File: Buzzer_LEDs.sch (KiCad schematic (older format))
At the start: 24 parts, among them Q1 2N7002BK, Q2 BS250P

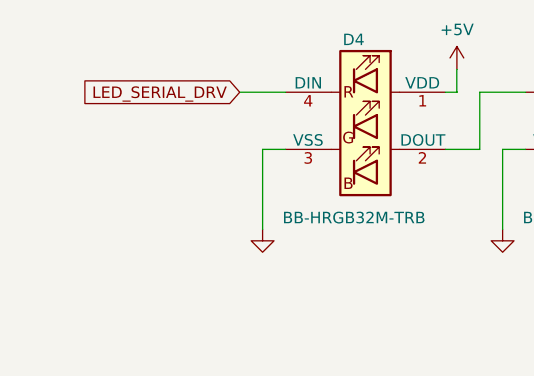
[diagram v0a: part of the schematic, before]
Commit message: changed label on LED Drive for 5V
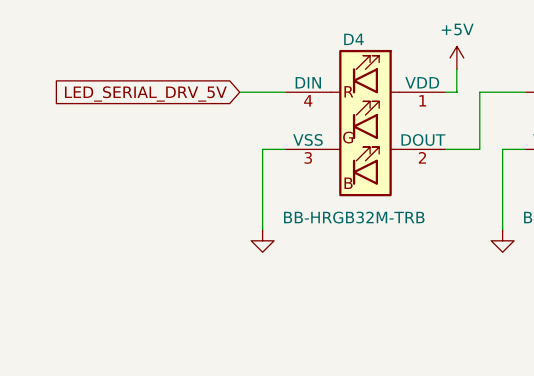
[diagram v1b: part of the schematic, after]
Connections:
- net LED_SERIAL_DRV renamed LED_SERIAL_DRV_5V
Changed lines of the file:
@@
 	2900 1875 2750 1875
 Text GLabel 1850 1625 0    50   Input ~ 0
-LED_SERIAL_DRV
+LED_SERIAL_DRV_5V
 Wire Wire Line
 	2050 1625 1850 1625

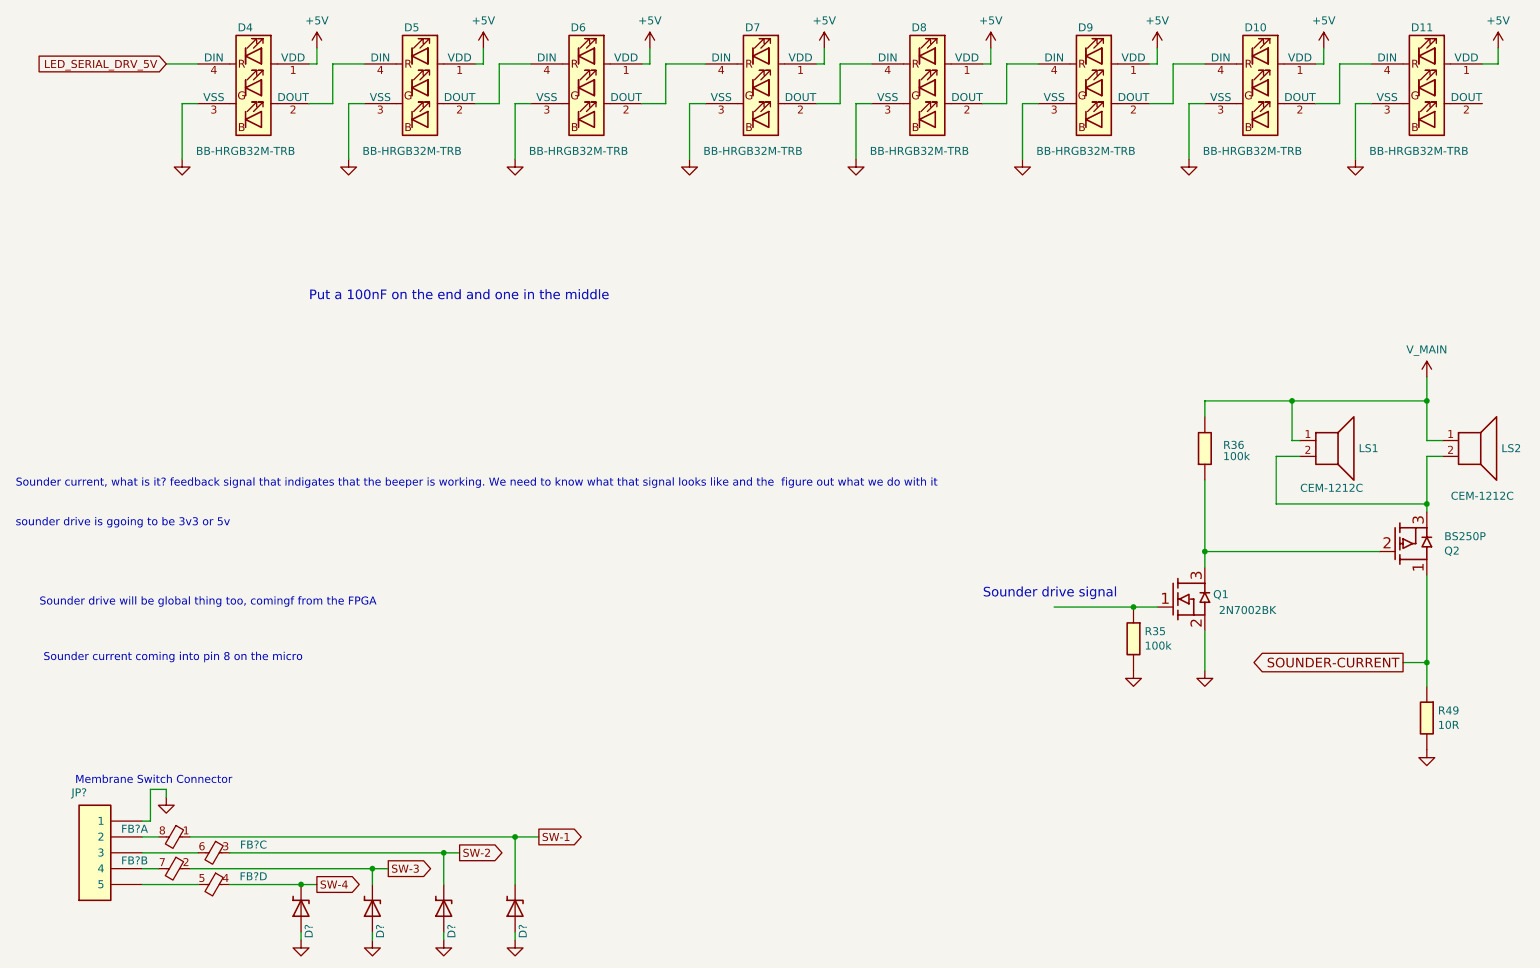
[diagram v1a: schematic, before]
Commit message: Push button signals SW-1 to SW-4 renamed with functional names, PB_MUTE etc
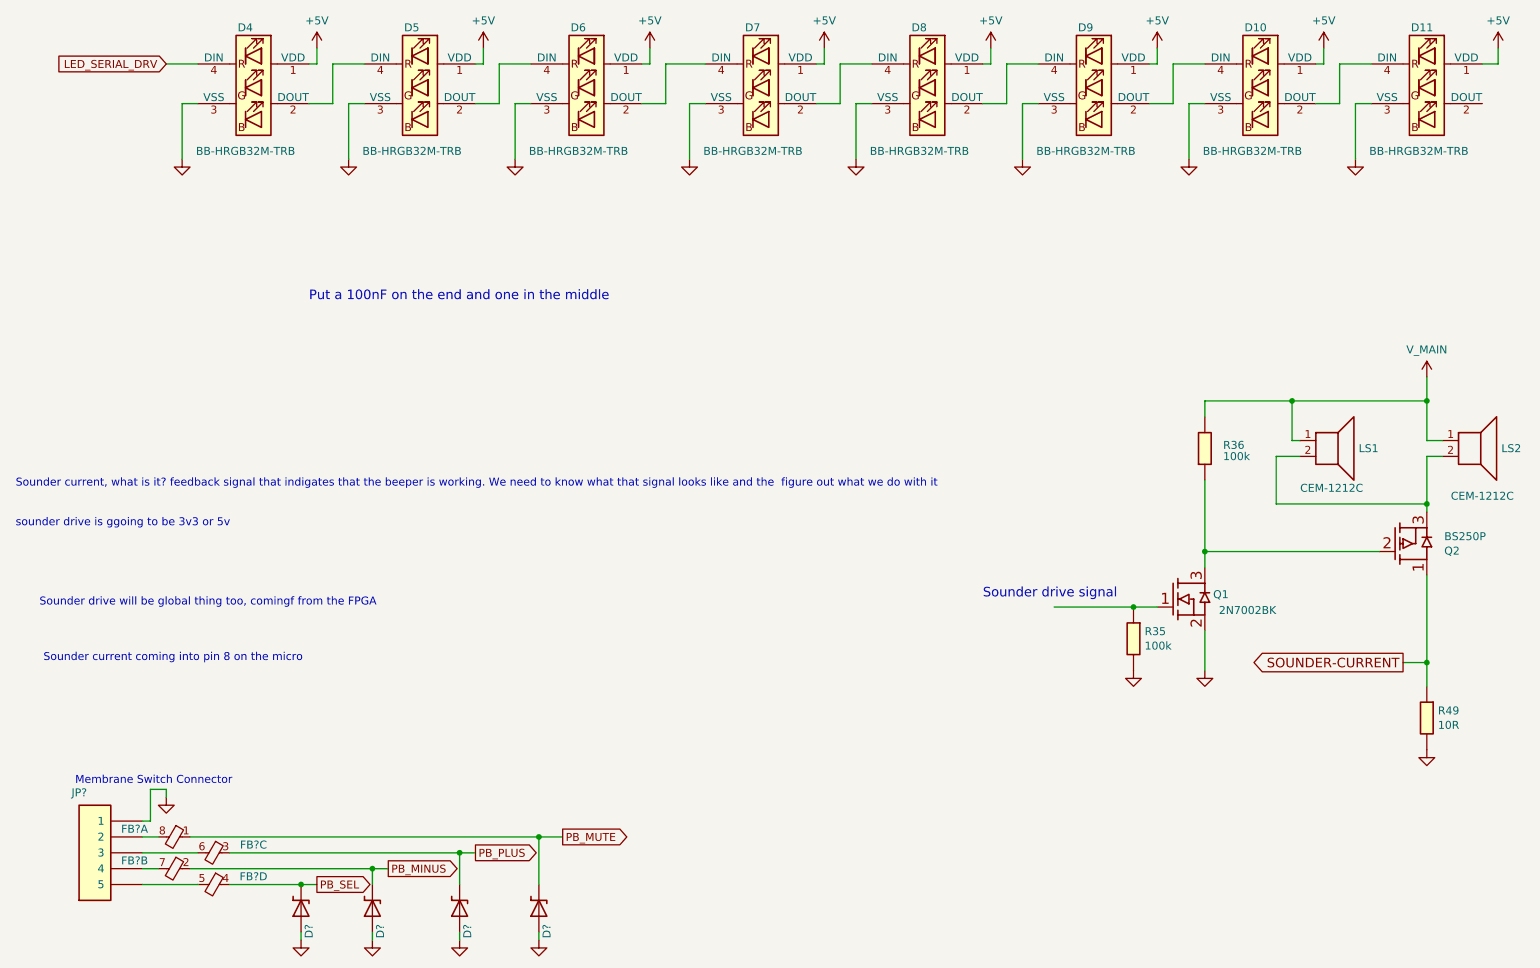
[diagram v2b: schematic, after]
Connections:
- net LED_SERIAL_DRV_5V renamed LED_SERIAL_DRV
- net SW-1 renamed PB_MUTE
- net SW-2 renamed PB_PLUS
- net SW-3 renamed PB_MINUS
- net SW-4 renamed PB_SEL
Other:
- moved on the sheet: D?
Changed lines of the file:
@@
 	2900 1875 2750 1875
 Text GLabel 1850 1625 0    50   Input ~ 0
-LED_SERIAL_DRV_5V
+LED_SERIAL_DRV
 Wire Wire Line
 	2050 1625 1850 1625
@@
 L OpenVent:SP3522-01UTG D?
 U 1 1 6040469D
-P 3600 6950
+P 3700 6950
 AR Path="/5F988182/600DF349" Ref="D?"  Part="1"
 AR Path="/5F8F894A/600DF349" Ref="D?"  Part="1"
 AR Path="/5F8F894A/6040469D" Ref="D?"  Part="1"
 AR Path="/5FCA4074/6040469D" Ref="D?"  Part="1"
-F 0 "D?" H 3500 6900 50  0000 R CNN
-F 1 "SP3522-01UTG" H 3725 6825 50  0001 R CNN
-F 2 "0603 diode" H 3650 7150 50  0001 C CNN
-F 3 "https://www.vishay.com/docs/85734/mmbd914.pdf" H 3600 6950 50  0001 C CNN
-F 4 "ESD Suppressors / TVS Diodes 1 Ch 22kV 9.2V .15pF 0603" H 3600 6650 50  0001 C CNN "Detailed"
-	1    3600 6950
+F 0 "D?" H 3600 6900 50  0000 R CNN
+F 1 "SP3522-01UTG" H 3825 6825 50  0001 R CNN
+F 2 "0603 diode" H 3750 7150 50  0001 C CNN
+F 3 "https://www.vishay.com/docs/85734/mmbd914.pdf" H 3700 6950 50  0001 C CNN
+F 4 "ESD Suppressors / TVS Diodes 1 Ch 22kV 9.2V .15pF 0603" H 3700 6650 50  0001 C CNN "Detailed"
+	1    3700 6950
 	0    -1   -1   0
 $EndComp
@@
 L OpenVent:SP3522-01UTG D?
 U 1 1 604046A4
-P 4050 6950
+P 4200 6950
 AR Path="/5F988182/604046A4" Ref="D?"  Part="1"
 AR Path="/5F8F894A/604046A4" Ref="D?"  Part="1"
 AR Path="/5FCA4074/604046A4" Ref="D?"  Part="1"
-F 0 "D?" H 3950 6900 50  0000 R CNN
-F 1 "SP3522-01UTG" H 4175 6825 50  0001 R CNN
-F 2 "0603 diode" H 4100 7150 50  0001 C CNN
-F 3 "https://www.vishay.com/docs/85734/mmbd914.pdf" H 4050 6950 50  0001 C CNN
-F 4 "ESD Suppressors / TVS Diodes 1 Ch 22kV 9.2V .15pF 0603" H 4050 6650 50  0001 C CNN "Detailed"
-	1    4050 6950
+F 0 "D?" H 4100 6900 50  0000 R CNN
+F 1 "SP3522-01UTG" H 4325 6825 50  0001 R CNN
+F 2 "0603 diode" H 4250 7150 50  0001 C CNN
+F 3 "https://www.vishay.com/docs/85734/mmbd914.pdf" H 4200 6950 50  0001 C CNN
+F 4 "ESD Suppressors / TVS Diodes 1 Ch 22kV 9.2V .15pF 0603" H 4200 6650 50  0001 C CNN "Detailed"
+	1    4200 6950
 	0    -1   -1   0
 $EndComp
@@
 L OpenVent:GND #GND_?
 U 1 1 604046B6
-P 3600 7150
+P 3700 7150
 AR Path="/5F988182/604046B6" Ref="#GND_?"  Part="1"
 AR Path="/5F8F894A/604046B6" Ref="#GND_?"  Part="1"
 AR Path="/5FCA4074/604046B6" Ref="#GND_?"  Part="1"
-F 0 "#GND_?" H 3600 7150 20  0001 C CNN
-F 1 "GND" H 3600 7080 50  0001 C CNN
-F 2 "" H 3600 7150 70  0001 C CNN
-F 3 "" H 3600 7150 70  0001 C CNN
-	1    3600 7150
+F 0 "#GND_?" H 3700 7150 20  0001 C CNN
+F 1 "GND" H 3700 7080 50  0001 C CNN
+F 2 "" H 3700 7150 70  0001 C CNN
+F 3 "" H 3700 7150 70  0001 C CNN
+	1    3700 7150
 	1    0    0    -1
 $EndComp
@@
 L OpenVent:GND #GND_?
 U 1 1 604046BC
-P 4050 7150
+P 4200 7150
 AR Path="/5F988182/604046BC" Ref="#GND_?"  Part="1"
 AR Path="/5F8F894A/604046BC" Ref="#GND_?"  Part="1"
 AR Path="/5FCA4074/604046BC" Ref="#GND_?"  Part="1"
-F 0 "#GND_?" H 4050 7150 20  0001 C CNN
-F 1 "GND" H 4050 7080 50  0001 C CNN
-F 2 "" H 4050 7150 70  0001 C CNN
-F 3 "" H 4050 7150 70  0001 C CNN
-	1    4050 7150
-	1    0    0    -1
-$EndComp
-Text GLabel 4200 6500 2    50   Output ~ 0
-SW-1
-Text GLabel 3700 6600 2    50   Output ~ 0
-SW-2
+F 0 "#GND_?" H 4200 7150 20  0001 C CNN
+F 1 "GND" H 4200 7080 50  0001 C CNN
+F 2 "" H 4200 7150 70  0001 C CNN
+F 3 "" H 4200 7150 70  0001 C CNN
+	1    4200 7150
+	1    0    0    -1
+$EndComp
+Text GLabel 4350 6500 2    50   Output ~ 0
+PB_MUTE
+Text GLabel 3800 6600 2    50   Output ~ 0
+PB_PLUS
 Text GLabel 3250 6700 2    50   Output ~ 0
-SW-3
+PB_MINUS
 Text GLabel 2800 6800 2    50   Output ~ 0
-SW-4
+PB_SEL
 $Comp
 L OpenVent:SP3522-01UTG D?
@@
 	1700 6800 2050 6800
 Wire Wire Line
-	2000 6500 4050 6500
-Wire Wire Line
-	2250 6600 3600 6600
-Wire Wire Line
 	3250 6700 3150 6700
 Wire Wire Line
@@
 	3150 6700 2000 6700
 Wire Wire Line
-	3600 6800 3600 6600
-Connection ~ 3600 6600
-Wire Wire Line
-	3600 6600 3700 6600
-Wire Wire Line
-	4050 6800 4050 6500
-Connection ~ 4050 6500
-Wire Wire Line
-	4050 6500 4200 6500
+	3700 6800 3700 6600
+Connection ~ 3700 6600
+Wire Wire Line
+	3700 6600 3800 6600
+Wire Wire Line
+	4200 6800 4200 6500
+Connection ~ 4200 6500
+Wire Wire Line
+	4200 6500 4350 6500
 Wire Wire Line
 	2700 7100 2700 7150
@@
 	3150 7100 3150 7150
 Wire Wire Line
-	3600 7100 3600 7150
-Wire Wire Line
-	4050 7100 4050 7150
+	3700 7100 3700 7150
+Wire Wire Line
+	4200 7100 4200 7150
+Wire Wire Line
+	2000 6500 4200 6500
+Wire Wire Line
+	2250 6600 3700 6600
 $EndSCHEMATC
